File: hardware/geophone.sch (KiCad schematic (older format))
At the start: 53 parts, among them P1 CONN_01X02, P2 CONN_01X02, P3 CONN_01X02, U1 ICL7660, U2 LMC6062, U5 FEATHER

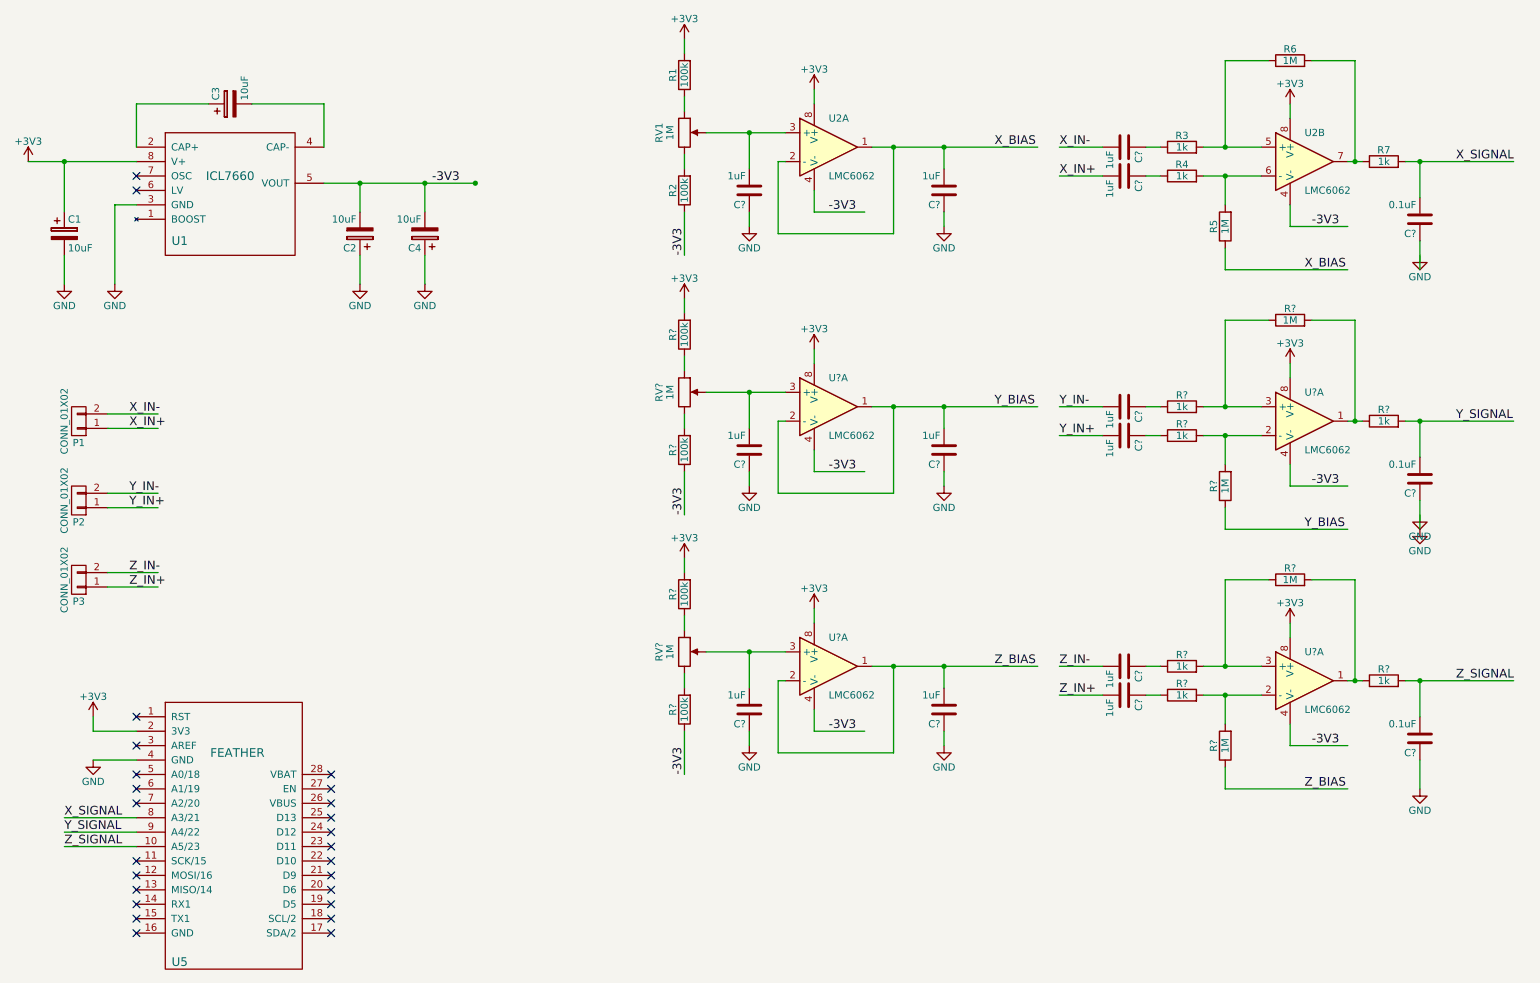
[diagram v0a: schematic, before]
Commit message: Adding some jumper locations for tweaking gain resistors.
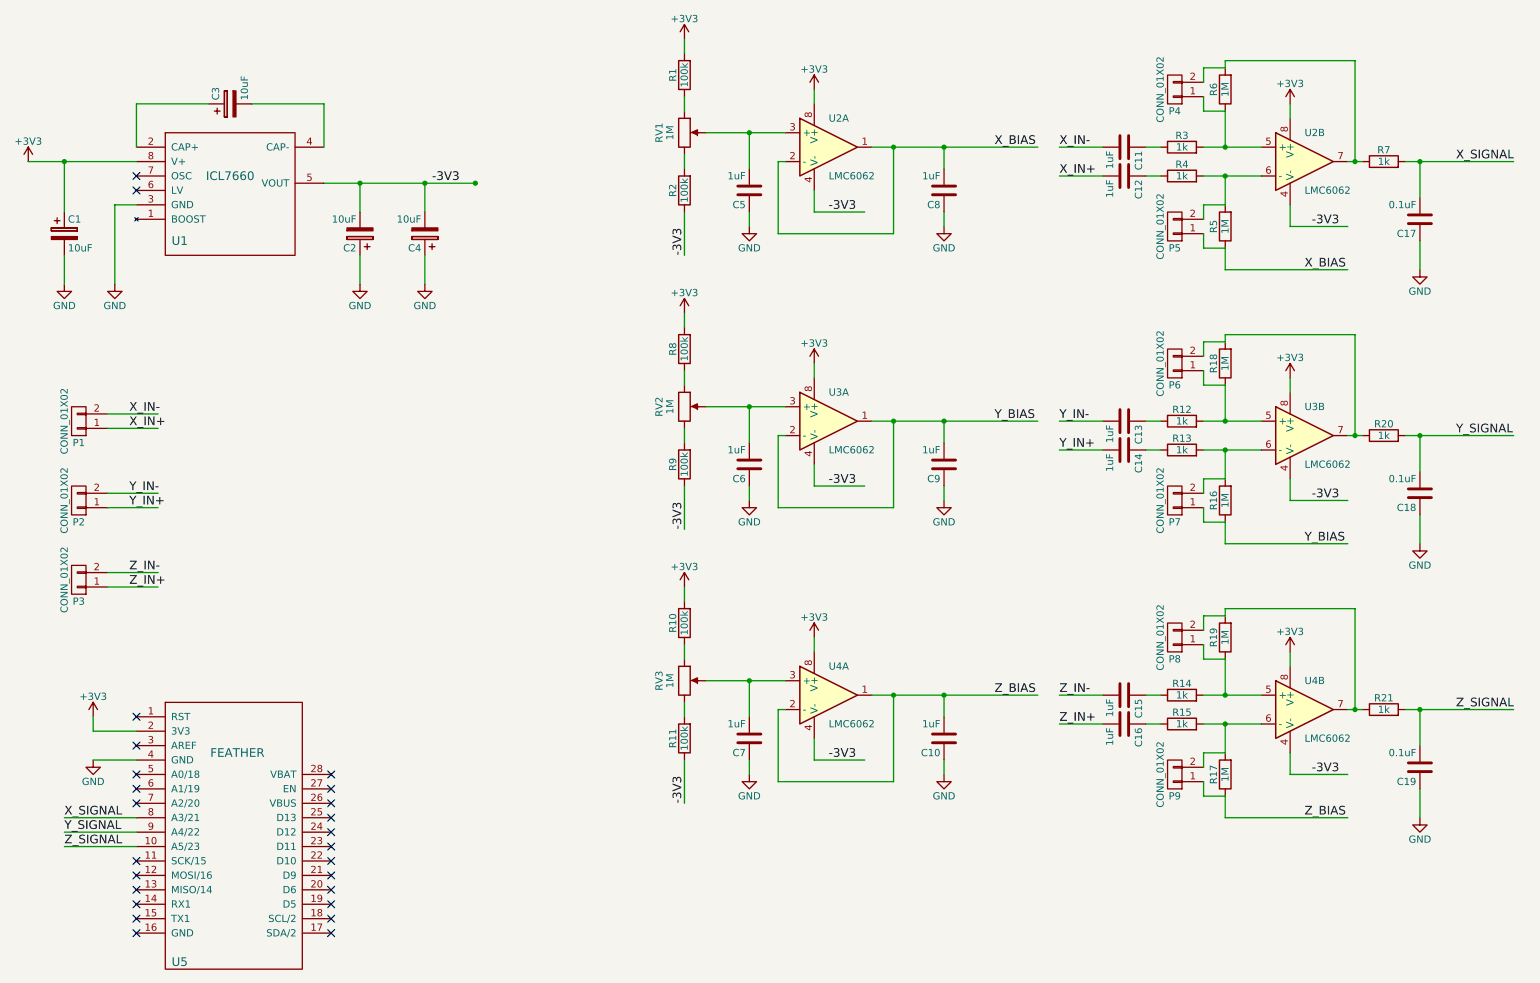
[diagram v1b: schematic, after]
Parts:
- added P4, P5, P6, P7, P8, P9: CONN_01X02, Socket_Strips:Socket_Strip_Straight_1x02_Pitch2.54mm, symbol CONN_01X02
- C1, C2, C3, C4: footprint Capacitors_ThroughHole:CP_Radial_D10.0mm_P5.00mm_P7.50mm -> Capacitors_THT:CP_Radial_D5.0mm_P2.00mm; SPN 493-7383-1-ND -> 493-12763-1-ND
- C10, C11, C12, C13, C14, C15, C16, C5, C6, C7, C8, C9: renamed from C?; footprint (none) -> Capacitors_THT:C_Disc_D6.0mm_W4.4mm_P5.00mm; SPN (none) -> 445-2884-ND
- C17, C18, C19: renamed from C?; footprint (none) -> Capacitors_THT:C_Disc_D6.0mm_W4.4mm_P5.00mm; SPN (none) -> 478-4855-ND
- P1, P2, P3: footprint Socket_Strips:Socket_Strip_Straight_1x02 -> Socket_Strips:Socket_Strip_Straight_1x02_Pitch2.54mm
- R1: footprint Resistors_ThroughHole:R_Axial_DIN0207_L6.3mm_D2.5mm_P10.16mm_Horizontal -> Resistors_THT:R_Axial_DIN0207_L6.3mm_D2.5mm_P10.16mm_Horizontal; SPN 2.2KQBK-ND -> CF14JT100KCT-ND
- R10, R8: renamed from R?; footprint Resistors_ThroughHole:R_Axial_DIN0207_L6.3mm_D2.5mm_P10.16mm_Horizontal -> Resistors_THT:R_Axial_DIN0207_L6.3mm_D2.5mm_P10.16mm_Horizontal; SPN 2.2KQBK-ND -> CF14JT100KCT-ND
- R11, R9: renamed from R?; footprint Resistors_ThroughHole:R_Axial_DIN0207_L6.3mm_D2.5mm_P10.16mm_Horizontal -> Resistors_THT:R_Axial_DIN0207_L6.3mm_D2.5mm_P10.16mm_Horizontal; SPN CF14JT180KCT-ND -> CF14JT100KCT-ND
- R12, R13, R14, R15, R20, R21: renamed from R?; footprint Resistors_ThroughHole:R_Axial_DIN0207_L6.3mm_D2.5mm_P10.16mm_Horizontal -> Resistors_THT:R_Axial_DIN0207_L6.3mm_D2.5mm_P10.16mm_Horizontal; SPN 2.2KQBK-ND -> CF14JT1K00CT-ND
- R16, R17, R18, R19: renamed from R?; footprint Resistors_ThroughHole:R_Axial_DIN0207_L6.3mm_D2.5mm_P10.16mm_Horizontal -> Resistors_THT:R_Axial_DIN0207_L6.3mm_D2.5mm_P10.16mm_Horizontal; SPN 2.2KQBK-ND -> CF14JT1M00CT-ND
- R2: footprint Resistors_ThroughHole:R_Axial_DIN0207_L6.3mm_D2.5mm_P10.16mm_Horizontal -> Resistors_THT:R_Axial_DIN0207_L6.3mm_D2.5mm_P10.16mm_Horizontal; SPN CF14JT180KCT-ND -> CF14JT100KCT-ND
- R3, R4, R7: footprint Resistors_ThroughHole:R_Axial_DIN0207_L6.3mm_D2.5mm_P10.16mm_Horizontal -> Resistors_THT:R_Axial_DIN0207_L6.3mm_D2.5mm_P10.16mm_Horizontal; SPN 2.2KQBK-ND -> CF14JT1K00CT-ND
- R5, R6: footprint Resistors_ThroughHole:R_Axial_DIN0207_L6.3mm_D2.5mm_P10.16mm_Horizontal -> Resistors_THT:R_Axial_DIN0207_L6.3mm_D2.5mm_P10.16mm_Horizontal; SPN 2.2KQBK-ND -> CF14JT1M00CT-ND
- U2: footprint (none) -> Housings_DIP:DIP-8_W7.62mm_LongPads; SPN (none) -> LMC6482IN/NOPB-ND
- U3, U4: renamed from U?; footprint (none) -> Housings_DIP:DIP-8_W7.62mm_LongPads; SPN (none) -> LMC6482IN/NOPB-ND
- U4: renamed from U?; footprint (none) -> Housings_DIP:DIP-8_W7.62mm_LongPads; SPN (none) -> CF14JT1M00CT-ND
- gave numbers to parts that had none: 2
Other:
- moved on the sheet: C10, C13, C14, C15, C16, C18, C19, C6, C7, C9, R10, R11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
